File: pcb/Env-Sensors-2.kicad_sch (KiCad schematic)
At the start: 17 parts, among them Q1 MMBFJ201, U11 BMP581, U12 MCP6042, U13 ADS1115, U16 TGS5141, U17 DS18S20, U8 TSL2591

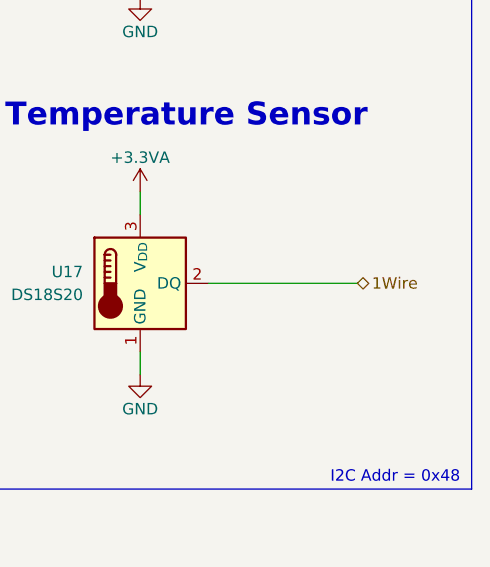
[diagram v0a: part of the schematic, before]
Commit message: BOM Updates
No PCB changes. This is still Rev.B
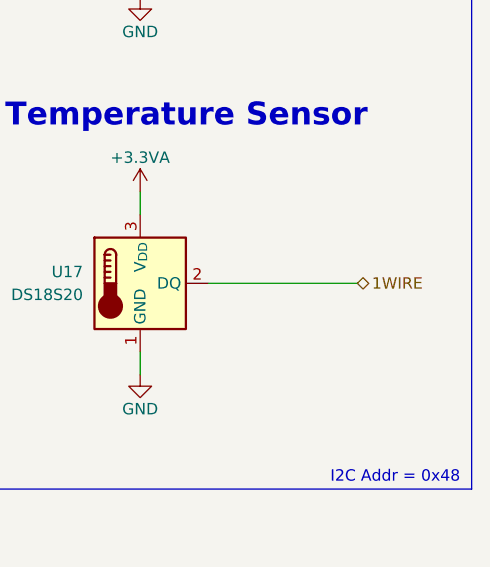
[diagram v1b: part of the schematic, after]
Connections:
- net 1Wire renamed 1WIRE
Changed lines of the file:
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@@
 		)
 	)
-	(hierarchical_label "1Wire"
+	(hierarchical_label "1WIRE"
 		(shape bidirectional)
 		(at 233.68 107.95 0)
